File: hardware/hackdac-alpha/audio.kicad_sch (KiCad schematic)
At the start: 24 parts, among them J4 I2C, J5 AUDIO OUT, P2 P22, Q5 2N7002, Q6 2N7002, U8 MCP1700T-3302E/MB, U9 PCM5102

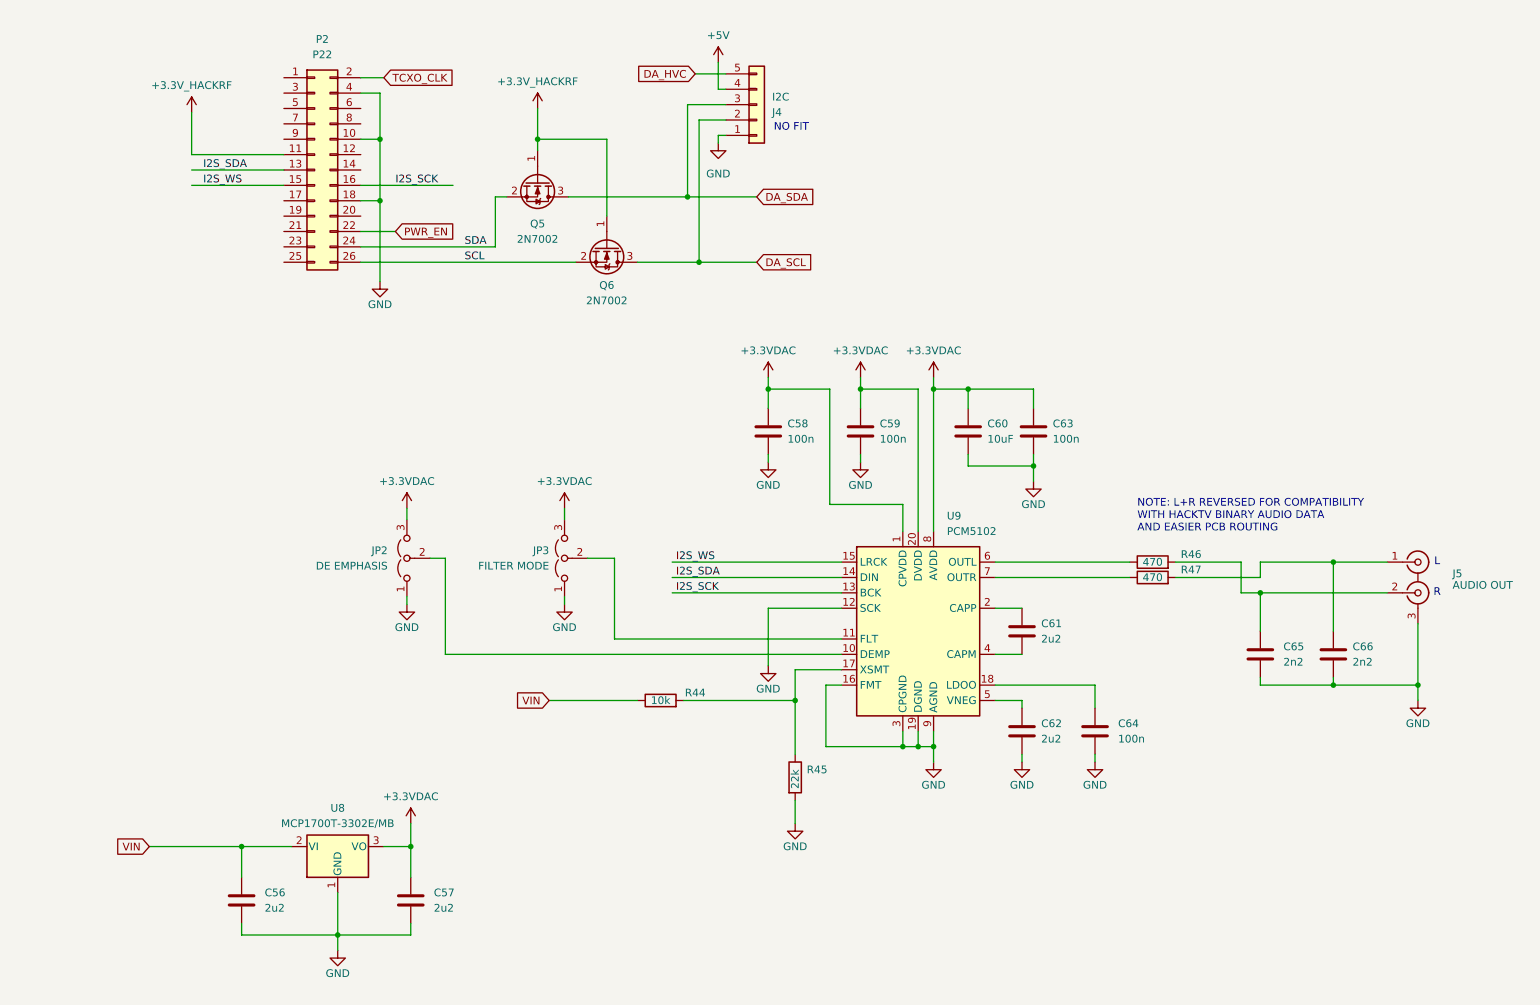
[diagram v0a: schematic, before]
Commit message: Modify I2C buffering to allow power-down of HackDAC
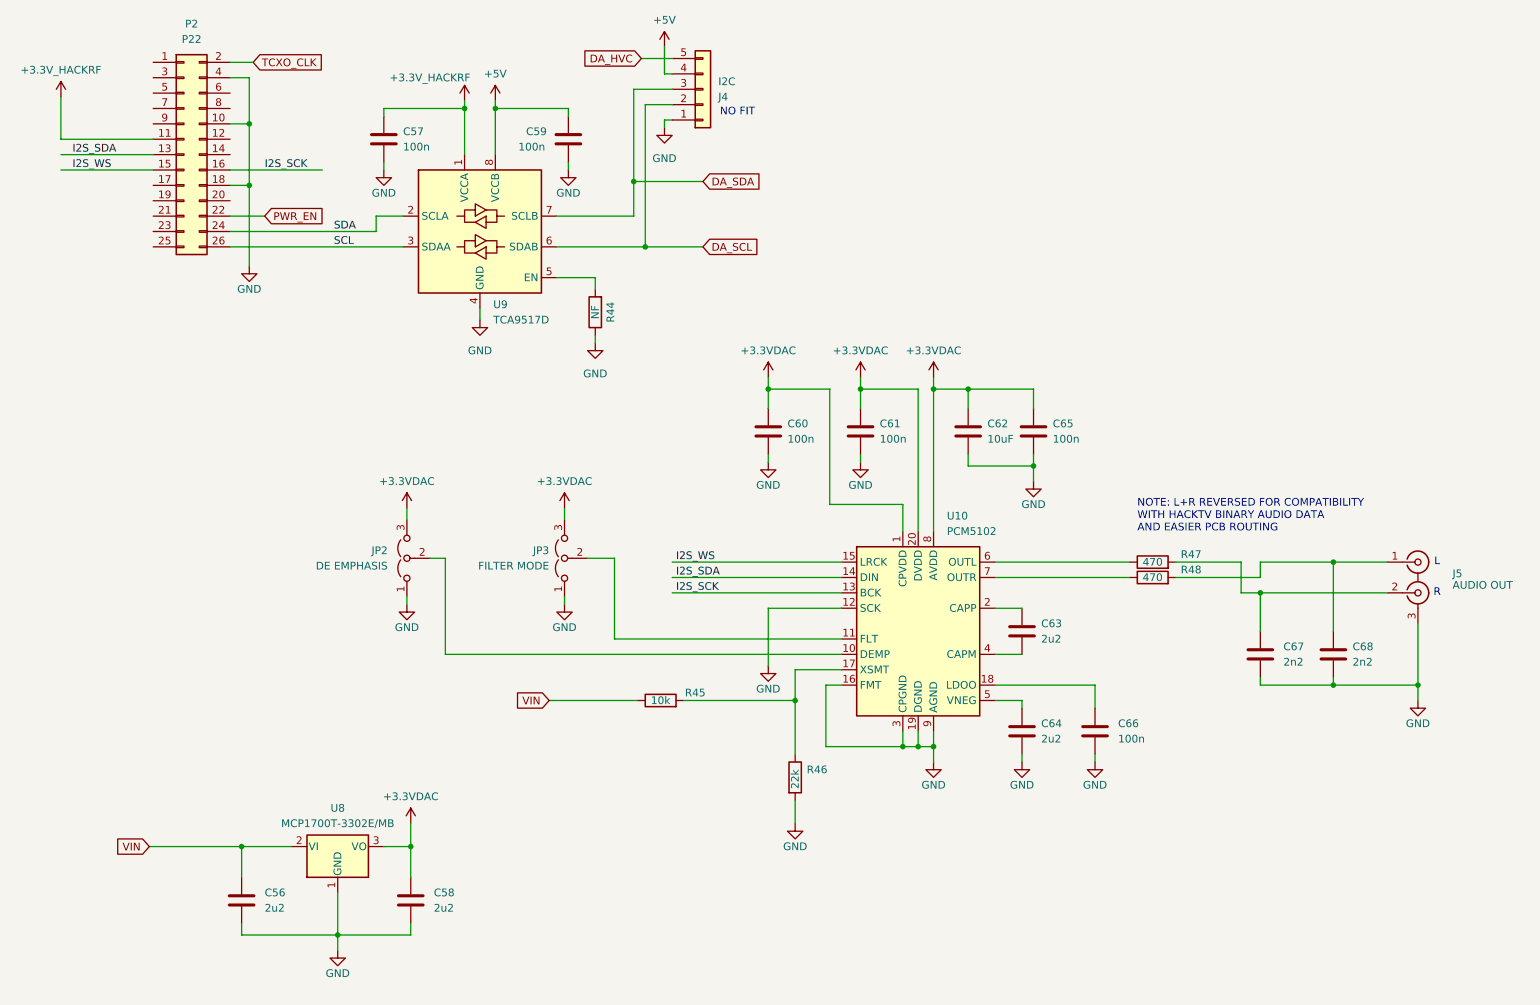
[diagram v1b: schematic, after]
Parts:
- removed Q5, Q6: 2N7002, Package_TO_SOT_SMD:SOT-23, symbol Transistor_FET:2N7002
- added C57, C59: 100n, Capacitor_SMD:C_0603_1608Metric, symbol Device:C
- added R44: NF, Resistor_SMD:R_0603_1608Metric, symbol Device:R
- added U9: TCA9517D, Package_SO:SOIC-8_3.9x4.9mm_P1.27mm, symbol Logic_LevelTranslator:TCA9517D
- renumbered C57 to C58, C58 to C60, C59 to C61, C60 to C62, C61 to C63, C62 to C64, C63 to C65, C64 to C66, C65 to C67, C66 to C68, R44 to R45, R45 to R46, R46 to R47, R47 to R48, U9 to U10
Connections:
- net +3.3V_HACKRF: now also C57.1, U9.1 (VCCA)
- net +5V: now also C59.1, U9.8 (VCCB)
- net DA_SCL: now also U9.6 (SDAB)
- net DA_SDA: now also U9.7 (SCLB)
- net GND: now also C57.2, C59.2, R44.1, U9.4 (GND)
- net SCL: now also U9.3 (SDAA)
- net SDA: now also U9.2 (SCLA)
- new net: R44.2, U9.5 (EN)
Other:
- moved on the sheet: J4, P2

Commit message: Changed X1 to 5x3.2mm footprint
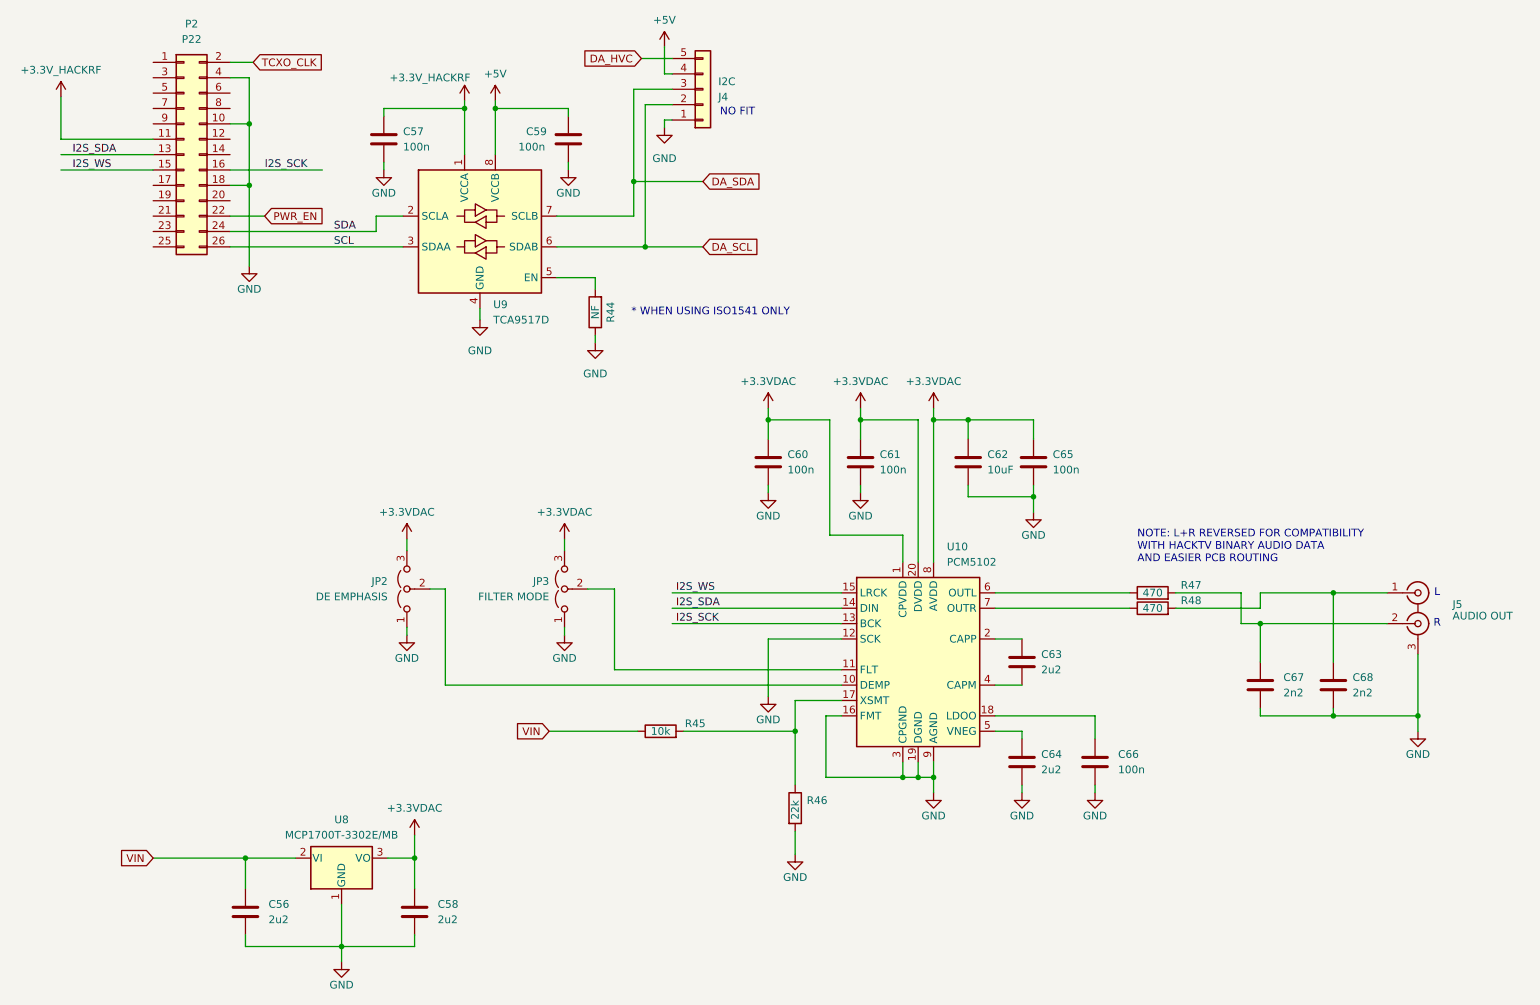
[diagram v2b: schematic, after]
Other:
- note added: "* WHEN USING ISO1541 ONLY"
- moved on the sheet: C56, C58, C60, C61, C62, C63, C64, C65, C66, C67, C68, J5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

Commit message: Add jumper to configure sync out connector
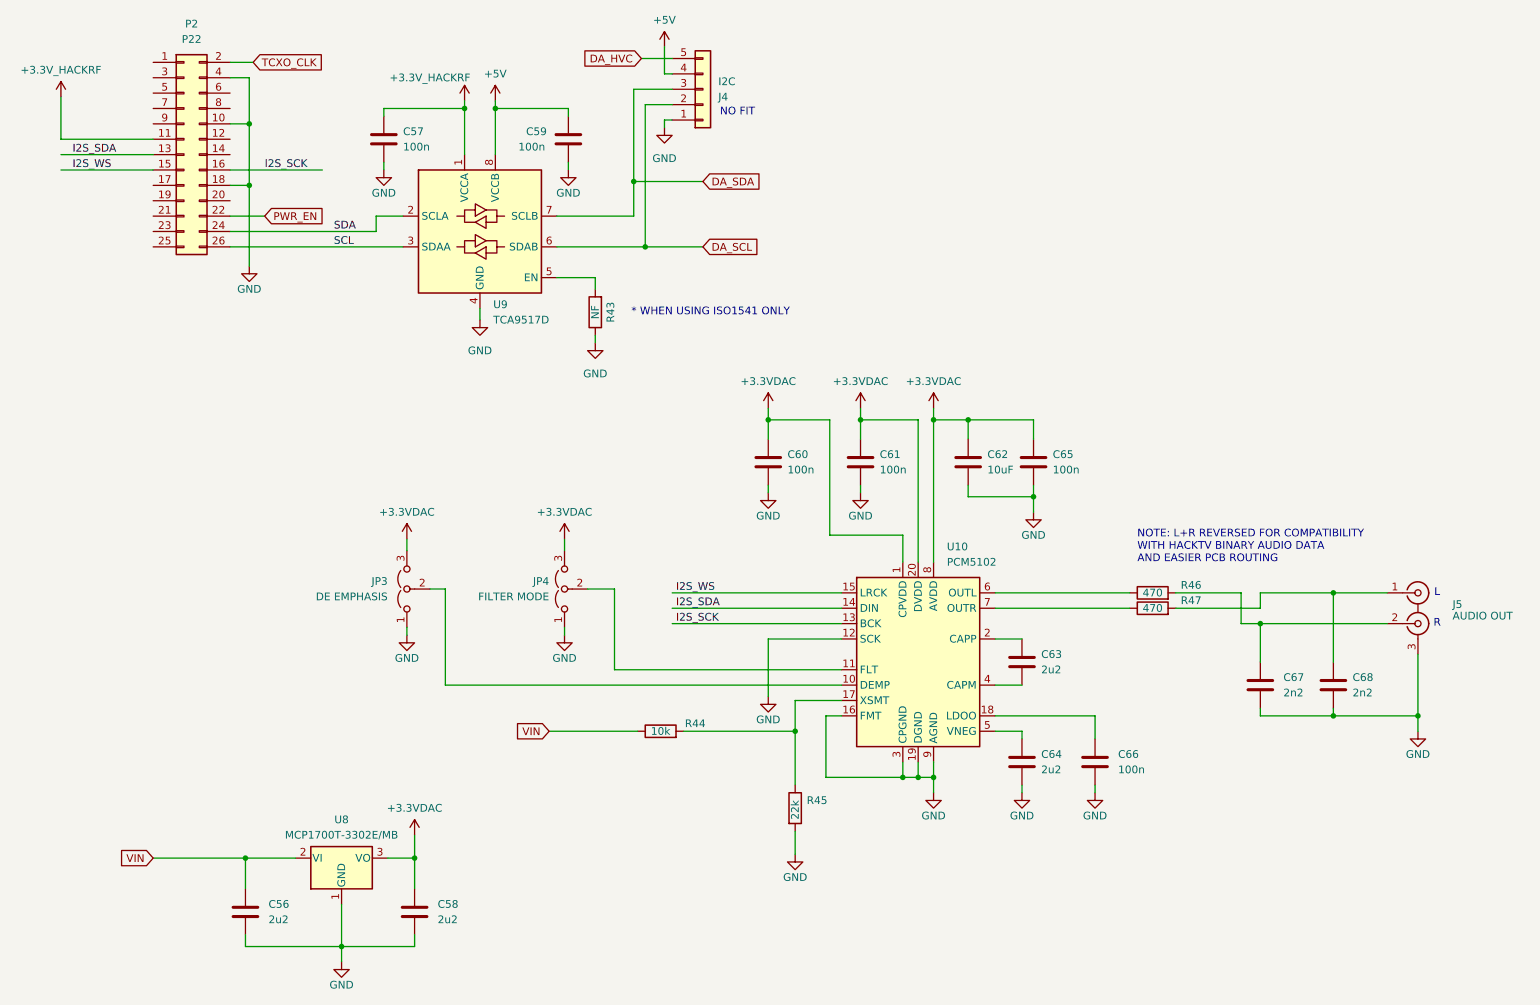
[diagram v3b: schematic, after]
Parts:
- renumbered JP2 to JP3, JP3 to JP4, R44 to R43, R45 to R44, R46 to R45, R47 to R46, R48 to R47
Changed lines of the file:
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@@
 		(on_board yes)
 		(dnp no)
-		(property "Reference" "R48"
+		(property "Reference" "R47"
 			(at 213.36 116.205 90)
 			(effects
@@
 			(project "dacattac-alpha"
 				(path "/487245ca-0c1f-4f9d-bc99-20c8f558090f/80e17ed4-cb43-4c12-a09c-75e0f0ffaba0"
-					(reference "R48")
+					(reference "R47")
 					(unit 1)
 				)
@@
 		(dnp no)
 		(fields_autoplaced yes)
-		(property "Reference" "JP2"
+		(property "Reference" "JP3"
 			(at 80.645 113.03 90)
 			(effects
@@
 			(project "dacattac-alpha"
 				(path "/487245ca-0c1f-4f9d-bc99-20c8f558090f/80e17ed4-cb43-4c12-a09c-75e0f0ffaba0"
-					(reference "JP2")
+					(reference "JP3")
 					(unit 1)
 				)
@@
 		(on_board yes)
 		(dnp no)
-		(property "Reference" "R47"
+		(property "Reference" "R46"
 			(at 213.36 113.665 90)
 			(effects
@@
 			(project "dacattac-alpha"
 				(path "/487245ca-0c1f-4f9d-bc99-20c8f558090f/80e17ed4-cb43-4c12-a09c-75e0f0ffaba0"
-					(reference "R47")
+					(reference "R46")
 					(unit 1)
 				)
@@
 		(on_board yes)
 		(dnp no)
-		(property "Reference" "R45"
+		(property "Reference" "R44"
 			(at 131.445 136.525 90)
 			(effects
@@
 			(project "dacattac-alpha"
 				(path "/487245ca-0c1f-4f9d-bc99-20c8f558090f/80e17ed4-cb43-4c12-a09c-75e0f0ffaba0"
-					(reference "R45")
+					(reference "R44")
 					(unit 1)
 				)
@@
 		(on_board yes)
 		(dnp no)
-		(property "Reference" "R44"
+		(property "Reference" "R43"
 			(at 117.475 68.58 90)
 			(effects
@@
 			(project "hackdac-alpha"
 				(path "/487245ca-0c1f-4f9d-bc99-20c8f558090f/80e17ed4-cb43-4c12-a09c-75e0f0ffaba0"
-					(reference "R44")
+					(reference "R43")
 					(unit 1)
 				)
@@
 		(dnp no)
 		(fields_autoplaced yes)
-		(property "Reference" "JP3"
+		(property "Reference" "JP4"
 			(at 107.315 113.03 90)
 			(effects
@@
 			(project "dacattac-alpha"
 				(path "/487245ca-0c1f-4f9d-bc99-20c8f558090f/80e17ed4-cb43-4c12-a09c-75e0f0ffaba0"
-					(reference "JP3")
+					(reference "JP4")
 					(unit 1)
 				)
@@
 		(on_board yes)
 		(dnp no)
-		(property "Reference" "R46"
+		(property "Reference" "R45"
 			(at 149.86 149.225 0)
 			(effects
@@
 			(project "dacattac-alpha"
 				(path "/487245ca-0c1f-4f9d-bc99-20c8f558090f/80e17ed4-cb43-4c12-a09c-75e0f0ffaba0"
-					(reference "R46")
-					(unit 1)
-				)
+					(reference "R45")
+					(unit 1)
+				)
